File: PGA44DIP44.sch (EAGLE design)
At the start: 9 parts, among them CN1 JTAG, IC1 LM2937ET-3.3/NOPB

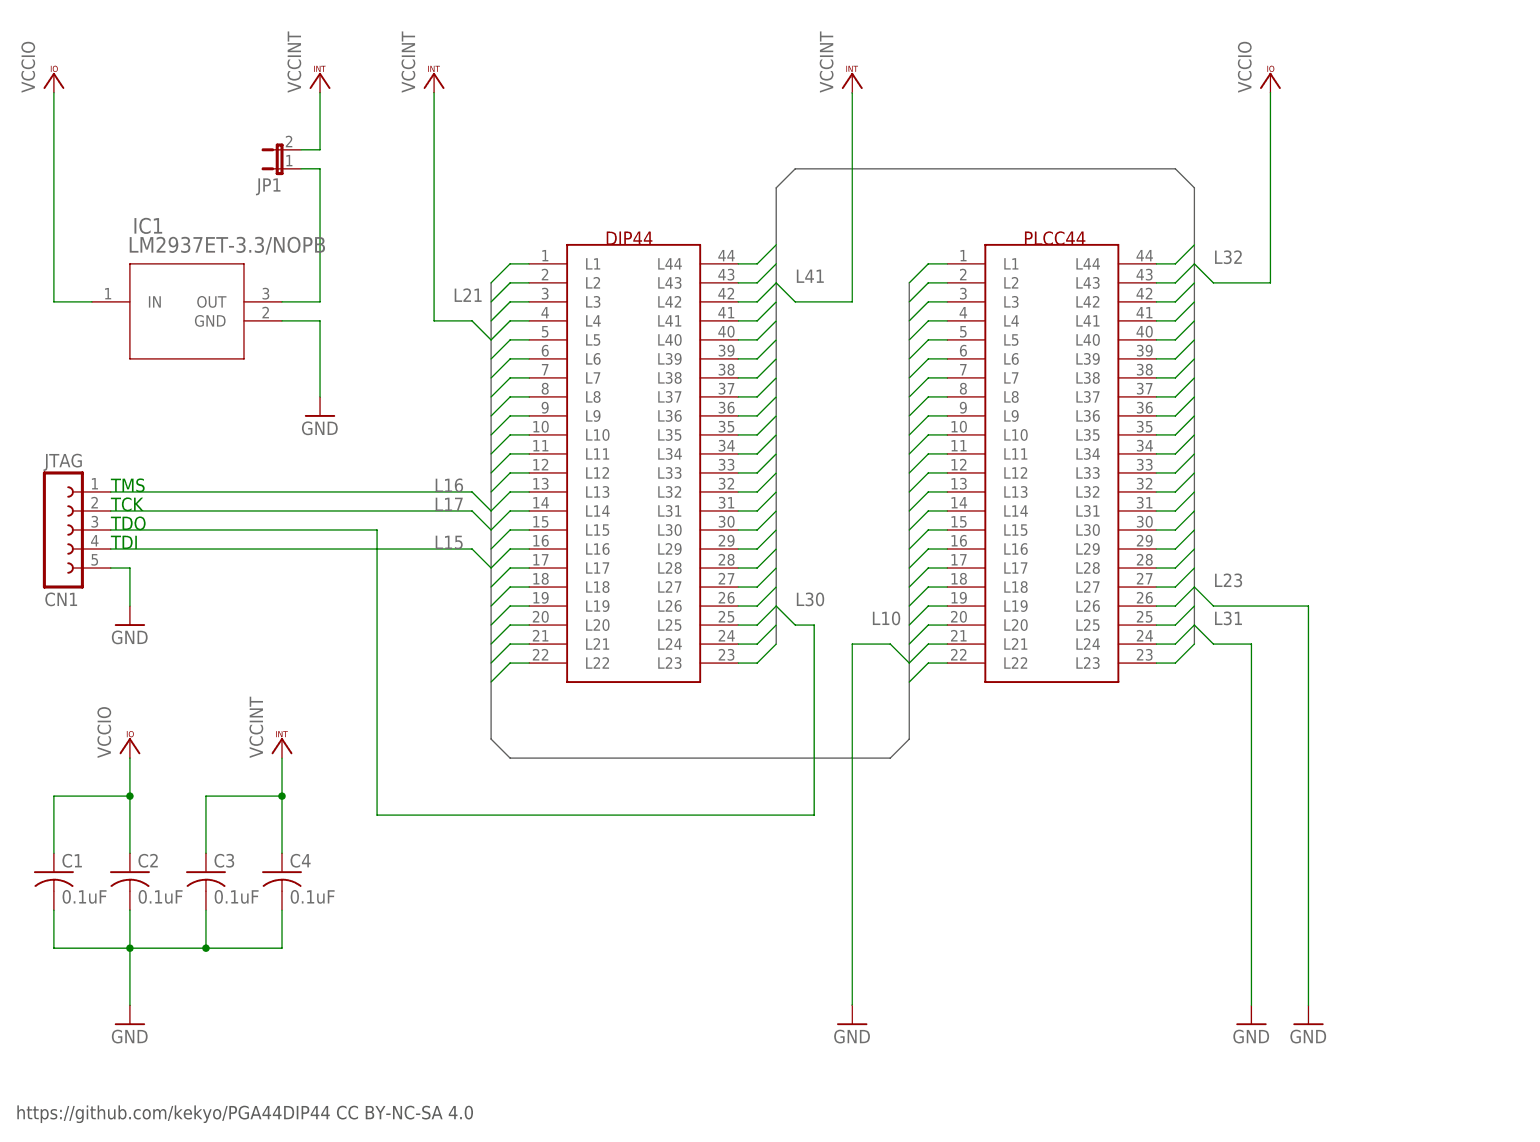
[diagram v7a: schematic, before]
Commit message: Fixed XC9572 version.
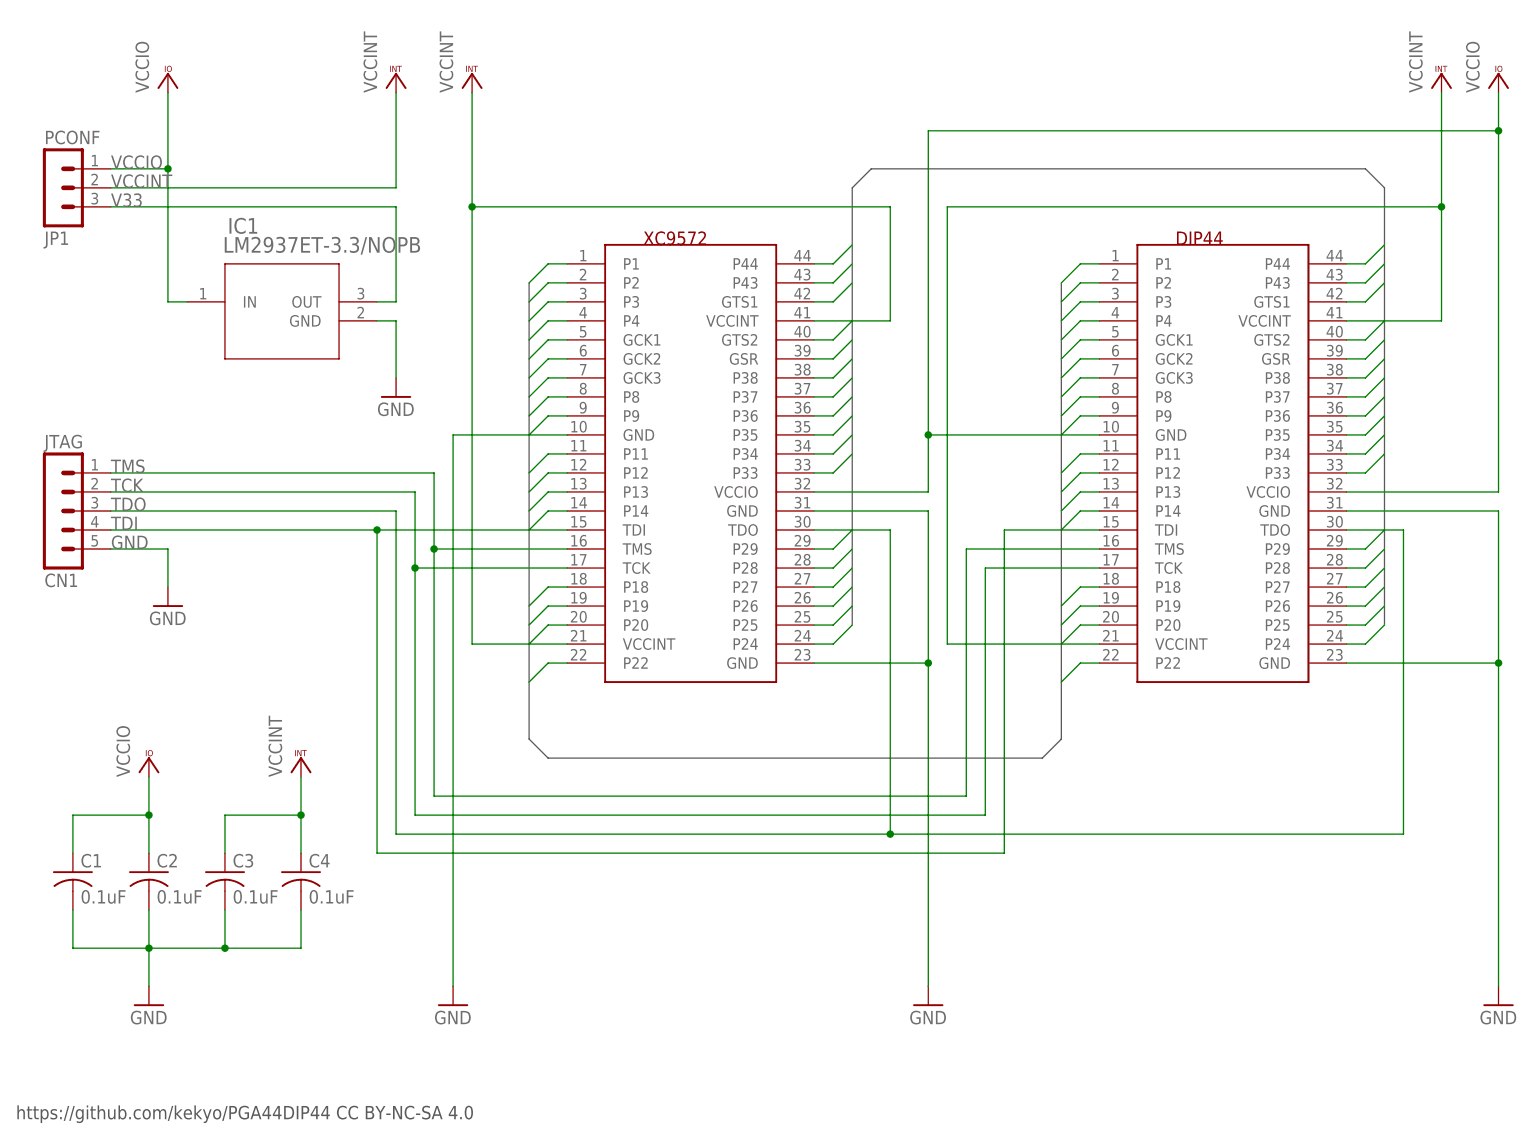
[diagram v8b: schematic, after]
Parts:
- removed PLCC44: PGA44, PGA44DIP44:PGA44
- added XC9572: PGA44, PGA44DIP44:PGA44
- CN1: device con-lsta:FE05-1 -> PGA44DIP44:MA05-1
- DIP44: value DIP44 -> (none)
- JP1: value (none) -> PCONF; device PGA44DIP44:JP1E -> PGA44DIP44:MA03-1
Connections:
- removed net L10: DIP44.L10, PLCC44.L10
- removed net L15: CN1.4, DIP44.L15, PLCC44.L15
- removed net L16: CN1.1, DIP44.L16, PLCC44.L16
- removed net L17: CN1.2, DIP44.L17, PLCC44.L17
- removed net L21: DIP44.L21, PLCC44.L21
- removed net L23: DIP44.L23, PLCC44.L23
- removed net L30: CN1.3, DIP44.L30, PLCC44.L30
- removed net L31: DIP44.L31, PLCC44.L31
- removed net L32: DIP44.L32, PLCC44.L32
- removed net L41: DIP44.L41, PLCC44.L41
- removed net N$1: IC1.OUT, JP1.1
- new net TCK: CN1.2, DIP44.TCK, XC9572.TCK
- new net TDI: CN1.4, DIP44.TDI, XC9572.TDI
- new net TDO: CN1.3, DIP44.TDO, XC9572.TDO
- new net TMS: CN1.1, DIP44.TMS, XC9572.TMS
- new net V33: IC1.OUT, JP1.3
- net GND: now also DIP44.GND@2, DIP44.GND@3, XC9572.GND@1, XC9572.GND@2, XC9572.GND@3
- net L1: now also DIP44.P1, XC9572.P1; no longer DIP44.L1, PLCC44.L1
- net L11: now also DIP44.P11, XC9572.P11; no longer DIP44.L11, PLCC44.L11
- net L12: now also DIP44.P12, XC9572.P12; no longer DIP44.L12, PLCC44.L12
- net L13: now also DIP44.P13, XC9572.P13; no longer DIP44.L13, PLCC44.L13
- net L14: now also DIP44.P14, XC9572.P14; no longer DIP44.L14, PLCC44.L14
- net L18: now also DIP44.P18, XC9572.P18; no longer DIP44.L18, PLCC44.L18
- net L19: now also DIP44.P19, XC9572.P19; no longer DIP44.L19, PLCC44.L19
- net L2: now also DIP44.P2, XC9572.P2; no longer DIP44.L2, PLCC44.L2
- net L20: now also DIP44.P20, XC9572.P20; no longer DIP44.L20, PLCC44.L20
- net L22: now also DIP44.P22, XC9572.P22; no longer DIP44.L22, PLCC44.L22
- net L24: now also DIP44.P24, XC9572.P24; no longer DIP44.L24, PLCC44.L24
- net L25: now also DIP44.P25, XC9572.P25; no longer DIP44.L25, PLCC44.L25
- net L26: now also DIP44.P26, XC9572.P26; no longer DIP44.L26, PLCC44.L26
- net L27: now also DIP44.P27, XC9572.P27; no longer DIP44.L27, PLCC44.L27
- net L28: now also DIP44.P28, XC9572.P28; no longer DIP44.L28, PLCC44.L28
- net L29: now also DIP44.P29, XC9572.P29; no longer DIP44.L29, PLCC44.L29
- net L3: now also DIP44.P3, XC9572.P3; no longer DIP44.L3, PLCC44.L3
- net L33: now also DIP44.P33, XC9572.P33; no longer DIP44.L33, PLCC44.L33
- net L34: now also DIP44.P34, XC9572.P34; no longer DIP44.L34, PLCC44.L34
- net L35: now also DIP44.P35, XC9572.P35; no longer DIP44.L35, PLCC44.L35
- net L36: now also DIP44.P36, XC9572.P36; no longer DIP44.L36, PLCC44.L36
- net L37: now also DIP44.P37, XC9572.P37; no longer DIP44.L37, PLCC44.L37
- net L38: now also DIP44.P38, XC9572.P38; no longer DIP44.L38, PLCC44.L38
- net L39: now also DIP44.GSR, XC9572.GSR; no longer DIP44.L39, PLCC44.L39
- net L4: now also DIP44.P4, XC9572.P4; no longer DIP44.L4, PLCC44.L4
- net L40: now also DIP44.GTS2, XC9572.GTS2; no longer DIP44.L40, PLCC44.L40
- net L42: now also DIP44.GTS1, XC9572.GTS1; no longer DIP44.L42, PLCC44.L42
- net L43: now also DIP44.P43, XC9572.P43; no longer DIP44.L43, PLCC44.L43
- net L44: now also DIP44.P44, XC9572.P44; no longer DIP44.L44, PLCC44.L44
- net L5: now also DIP44.GCK1, XC9572.GCK1; no longer DIP44.L5, PLCC44.L5
- net L6: now also DIP44.GCK2, XC9572.GCK2; no longer DIP44.L6, PLCC44.L6
- net L7: now also DIP44.GCK3, XC9572.GCK3; no longer DIP44.L7, PLCC44.L7
- net L8: now also DIP44.P8, XC9572.P8; no longer DIP44.L8, PLCC44.L8
- net L9: now also DIP44.P9, XC9572.P9; no longer DIP44.L9, PLCC44.L9
- net VCCINT: now also DIP44.VCCINT@1, DIP44.VCCINT@2, XC9572.VCCINT@1, XC9572.VCCINT@2
- net VCCIO: now also DIP44.GND@1, DIP44.VCCIO, JP1.1, XC9572.VCCIO
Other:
- note removed: "TCK"
- note removed: "TDI"
- note removed: "TDO"
- note removed: "TMS"
- moved on the sheet: C1, C2, C3, C4, CN1, DIP44, IC1
